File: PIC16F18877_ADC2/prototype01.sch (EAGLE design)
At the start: 35 parts, among them CN1 12V_IN, CN2 ADC_IN, CN3 UART_IF, CN4 PIC_CN_H, CN5 AE-MICRO-SD-DIP, CN6 I2C_IF, SW1 10-XX, U1 XC6202P332TH, U2 PIC16F18877-I/P, U3 AE-AQM1602A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

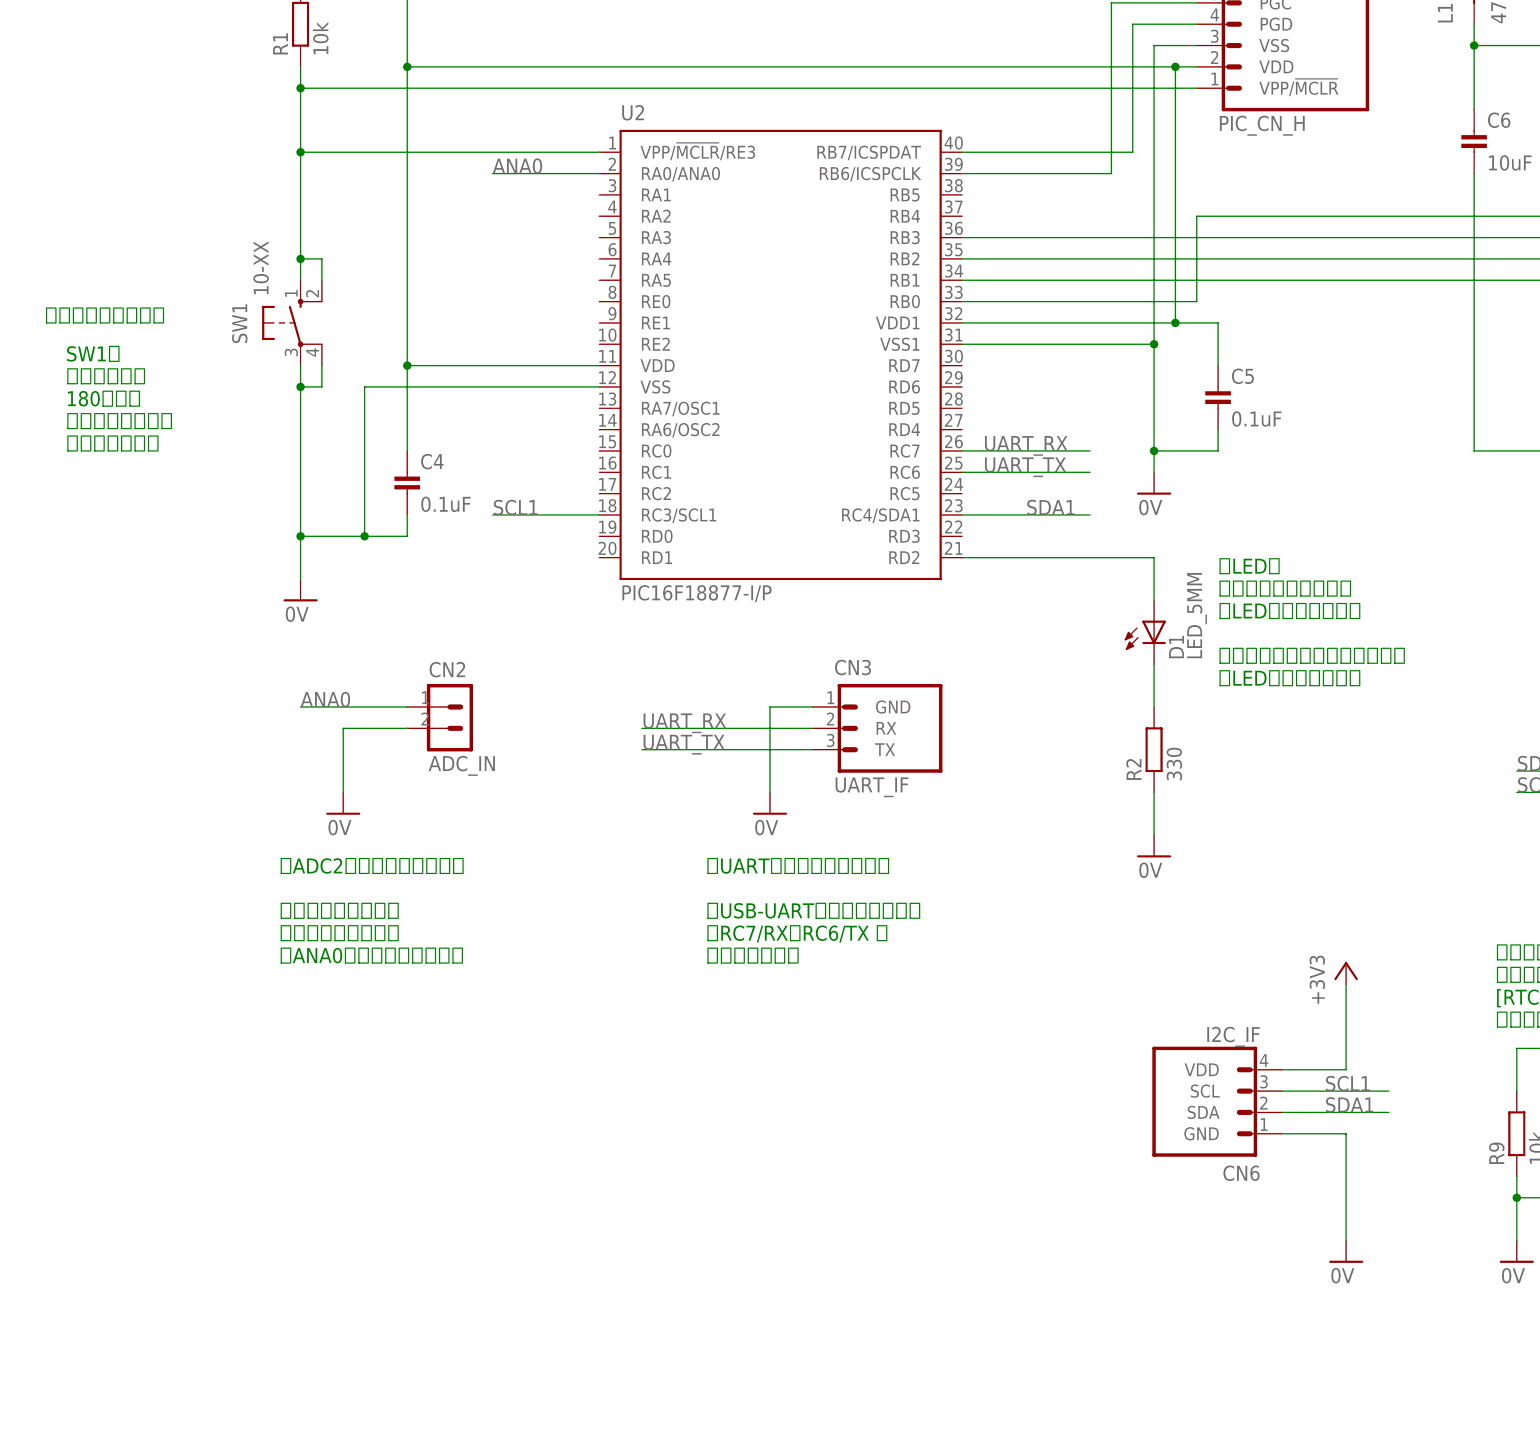
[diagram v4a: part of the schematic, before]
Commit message: 回路修正
・ANA0はポートごとの接続コネクターに集約するので一旦配線解除
・UART/I2C接続コネクターの説明コメントを修正
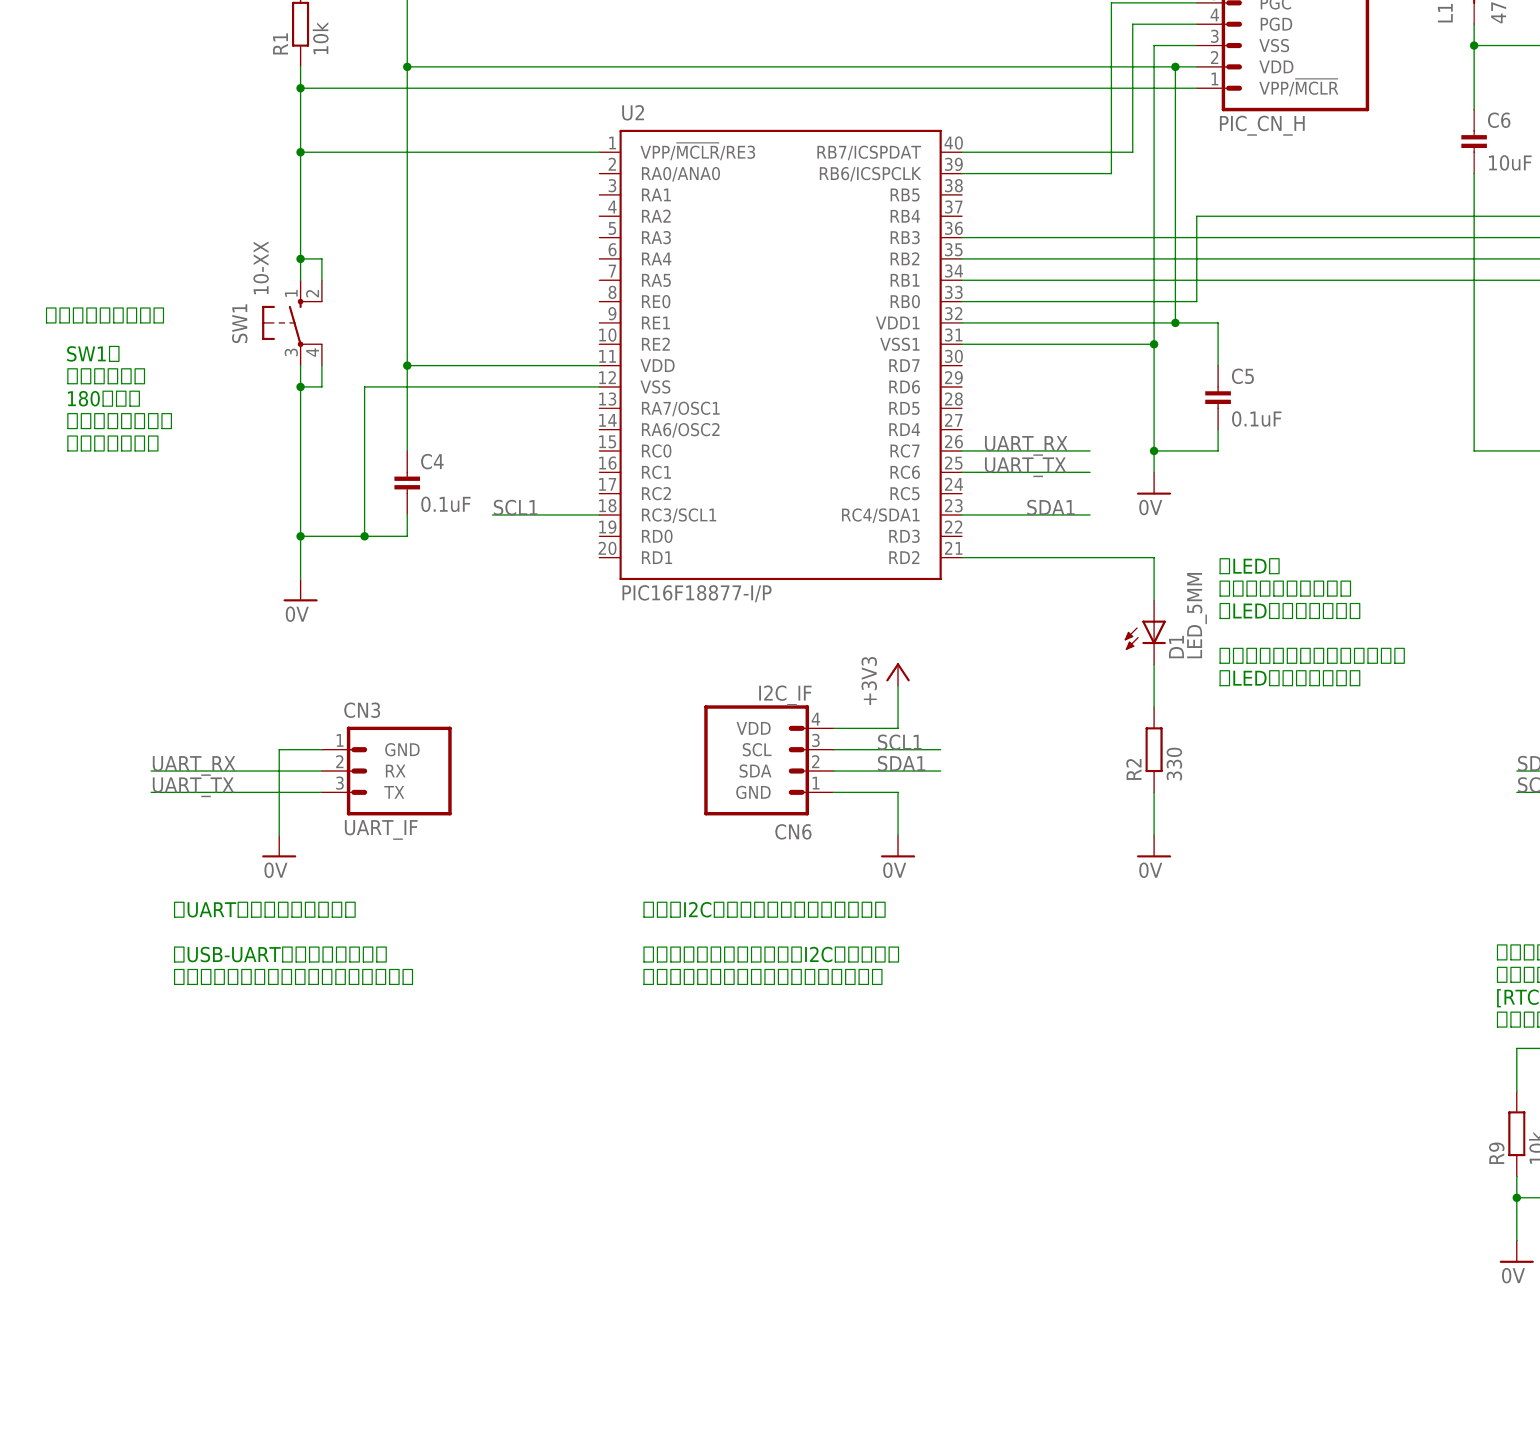
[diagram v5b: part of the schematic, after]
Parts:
- removed CN2: ADC_IN, Connectors:CONN_2PIN-L
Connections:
- removed net ANA0: CN2.1, U2.RA0/ANA0
- net 0V: no longer CN2.2
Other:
- note added: "【UART接続用コネクター】 USB-UART変換基板などを、 こちらのコネクターに接続できます。"
- note added: "【外部I2Cデバイス接続用コネクター】 温度センサーなどの外部I2Cデバイスを こちらのコネクターに接続できます。"
- note removed: "【ADC2のご使用について】 センサー等からの アナログ出力を、 ANA0端子に接続します。"
- note removed: "【UARTのご使用について】 USB-UART変換基板などを、 RC7/RX、RC6/TX に 接続します。"
- moved on the sheet: CN3, CN6
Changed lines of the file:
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@@
 <part name="SW1" library="Parts" deviceset="10-XX" device=""/>
 <part name="GND1" library="Supply" deviceset="0V" device=""/>
-<part name="CN2" library="Connectors" deviceset="CONN_2PIN" device="-L" value="ADC_IN"/>
-<part name="GND2" library="Supply" deviceset="0V" device=""/>
 <part name="H1" library="Generic" deviceset="MOUNT_HOLE" device="_3.2"/>
 <part name="H2" library="Generic" deviceset="MOUNT_HOLE" device="_3.2"/>
@@
 <sheet>
 <plain>
-<text x="177.8" y="93.98" size="1.778" layer="91">【UARTのご使用について】
+<text x="114.3" y="91.44" size="1.778" layer="91">【UART接続用コネクター】
 　USB-UART変換基板などを、
-　RC7/RX、RC6/TX に
-　接続します。</text>
+　こちらのコネクターに接続できます。</text>
 <text x="292.1" y="10.16" size="2.1844" layer="91">PIC16F18877 microSDサンプル
 小型LCD／RTCCを接続</text>
@@
  [AE-MICRO-SD-DIP]
 を使用します。</text>
-<text x="127" y="93.98" size="1.778" layer="91">【ADC2のご使用について】
-　センサー等からの
-　アナログ出力を、
-　ANA0端子に接続します。</text>
 <text x="238.76" y="127" size="1.778" layer="91">【LED】
 　カウントダウン中は
@@
 カウントダウンが
 開始されます。</text>
+<text x="170.18" y="91.44" size="1.778" layer="91">【外部I2Cデバイス接続用コネクター】
+　温度センサーなどの外部I2Cデバイスを
+　こちらのコネクターに接続できます。</text>
 </plain>
 <instances>
@@
 <instance part="SW1" gate="1" x="129.54" y="170.18"/>
 <instance part="GND1" gate="1" x="129.54" y="137.16"/>
-<instance part="CN2" gate="G$1" x="144.78" y="121.92"/>
-<instance part="GND2" gate="1" x="134.62" y="111.76"/>
 <instance part="H1" gate="G$1" x="312.42" y="38.1"/>
 <instance part="H2" gate="G$1" x="312.42" y="30.48"/>
@@
 <instance part="R6" gate="G$1" x="304.8" y="187.96" rot="R90"/>
 <instance part="C7" gate="G$1" x="312.42" y="165.1"/>
-<instance part="CN3" gate="G$1" x="190.5" y="124.46"/>
-<instance part="GND7" gate="1" x="185.42" y="111.76"/>
+<instance part="CN3" gate="G$1" x="132.08" y="119.38"/>
+<instance part="GND7" gate="1" x="127" y="106.68"/>
 <instance part="CN5" gate="G$1" x="320.04" y="185.42"/>
 <instance part="+3V1" gate="G$1" x="129.54" y="226.06"/>
@@
 <instance part="GND9" gate="1" x="327.66" y="58.42"/>
 <instance part="G1" gate="G$1" x="50.8" y="109.22" rot="R90"/>
-<instance part="CN6" gate="G$1" x="246.38" y="73.66" rot="R180"/>
-<instance part="+3V5" gate="G$1" x="254" y="93.98"/>
-<instance part="GND11" gate="1" x="254" y="58.42"/>
+<instance part="CN6" gate="G$1" x="193.04" y="114.3" rot="R180"/>
+<instance part="+3V5" gate="G$1" x="200.66" y="129.54"/>
+<instance part="GND11" gate="1" x="200.66" y="106.68"/>
 </instances>
 <busses>
@@
 </segment>
 <segment>
-<pinref part="CN2" gate="G$1" pin="2"/>
-<pinref part="GND2" gate="1" pin="0V"/>
-<wire x1="142.24" y1="121.92" x2="134.62" y2="121.92" width="0.1524" layer="91"/>
-<wire x1="134.62" y1="121.92" x2="134.62" y2="114.3" width="0.1524" layer="91"/>
-</segment>
-<segment>
 <pinref part="U3" gate="G$1" pin="GND"/>
 <pinref part="GND4" gate="1" pin="0V"/>
@@
 <pinref part="CN3" gate="G$1" pin="GND"/>
 <pinref part="GND7" gate="1" pin="0V"/>
-<wire x1="190.5" y1="124.46" x2="185.42" y2="124.46" width="0.1524" layer="91"/>
-<wire x1="185.42" y1="124.46" x2="185.42" y2="114.3" width="0.1524" layer="91"/>
+<wire x1="132.08" y1="119.38" x2="127" y2="119.38" width="0.1524" layer="91"/>
+<wire x1="127" y1="119.38" x2="127" y2="109.22" width="0.1524" layer="91"/>
 </segment>
 <segment>
@@
 <pinref part="CN6" gate="G$1" pin="GND"/>
 <pinref part="GND11" gate="1" pin="0V"/>
-<wire x1="246.38" y1="73.66" x2="254" y2="73.66" width="0.1524" layer="91"/>
-<wire x1="254" y1="73.66" x2="254" y2="60.96" width="0.1524" layer="91"/>
+<wire x1="193.04" y1="114.3" x2="200.66" y2="114.3" width="0.1524" layer="91"/>
+<wire x1="200.66" y1="114.3" x2="200.66" y2="109.22" width="0.1524" layer="91"/>
 </segment>
 </net>
@@
 </segment>
 </net>
-<net name="ANA0" class="0">
-<segment>
-<pinref part="U2" gate="G$1" pin="RA0/ANA0"/>
-<wire x1="165.1" y1="187.96" x2="152.4" y2="187.96" width="0.1524" layer="91"/>
-<label x="152.4" y="187.96" size="1.778" layer="95"/>
-</segment>
-<segment>
-<pinref part="CN2" gate="G$1" pin="1"/>
-<wire x1="142.24" y1="124.46" x2="129.54" y2="124.46" width="0.1524" layer="91"/>
-<label x="129.54" y="124.46" size="1.778" layer="95"/>
-</segment>
-</net>
 <net name="SCL1" class="0">
 <segment>
@@
 <segment>
 <pinref part="CN6" gate="G$1" pin="SCL"/>
-<wire x1="246.38" y1="78.74" x2="259.08" y2="78.74" width="0.1524" layer="91"/>
-<label x="251.46" y="78.74" size="1.778" layer="95"/>
+<wire x1="193.04" y1="119.38" x2="205.74" y2="119.38" width="0.1524" layer="91"/>
+<label x="198.12" y="119.38" size="1.778" layer="95"/>
 </segment>
 </net>
@@
 <segment>
 <pinref part="CN6" gate="G$1" pin="SDA"/>
-<wire x1="246.38" y1="76.2" x2="259.08" y2="76.2" width="0.1524" layer="91"/>
-<label x="251.46" y="76.2" size="1.778" layer="95"/>
+<wire x1="193.04" y1="116.84" x2="205.74" y2="116.84" width="0.1524" layer="91"/>
+<label x="198.12" y="116.84" size="1.778" layer="95"/>
 </segment>
 </net>
@@
 <segment>
 <pinref part="CN3" gate="G$1" pin="RX"/>
-<wire x1="190.5" y1="121.92" x2="170.18" y2="121.92" width="0.1524" layer="91"/>
-<label x="170.18" y="121.92" size="1.778" layer="95"/>
+<wire x1="132.08" y1="116.84" x2="111.76" y2="116.84" width="0.1524" layer="91"/>
+<label x="111.76" y="116.84" size="1.778" layer="95"/>
 </segment>
 <segment>
@@
 <segment>
 <pinref part="CN3" gate="G$1" pin="TX"/>
-<wire x1="190.5" y1="119.38" x2="170.18" y2="119.38" width="0.1524" layer="91"/>
-<label x="170.18" y="119.38" size="1.778" layer="95"/>
+<wire x1="132.08" y1="114.3" x2="111.76" y2="114.3" width="0.1524" layer="91"/>
+<label x="111.76" y="114.3" size="1.778" layer="95"/>
 </segment>
 <segment>
@@
 <segment>
 <pinref part="CN6" gate="G$1" pin="VDD"/>
-<wire x1="246.38" y1="81.28" x2="254" y2="81.28" width="0.1524" layer="91"/>
+<wire x1="193.04" y1="121.92" x2="200.66" y2="121.92" width="0.1524" layer="91"/>
 <pinref part="+3V5" gate="G$1" pin="+3V3"/>
-<wire x1="254" y1="81.28" x2="254" y2="91.44" width="0.1524" layer="91"/>
-</segment>
-</net>
+<wire x1="200.66" y1="121.92" x2="200.66" y2="127" width="0.1524" layer="91"/>
+</segment>
+</net>
